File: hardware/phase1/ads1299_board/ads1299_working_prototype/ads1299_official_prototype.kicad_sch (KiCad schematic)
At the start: 105 parts, among them J2 1725656, J3 TSM-110-01-T-DV-P-TR, J5 TSW-103-07-T-D, J6 36PIN_IDC, J80 Conn_02x16_Odd_Even, J81 Conn_02x16_Odd_Even, J9 1725656, U1 ADS1299IPAG, U10 24AA256-I/ST, U11 OPA376AID, U4 OPA376

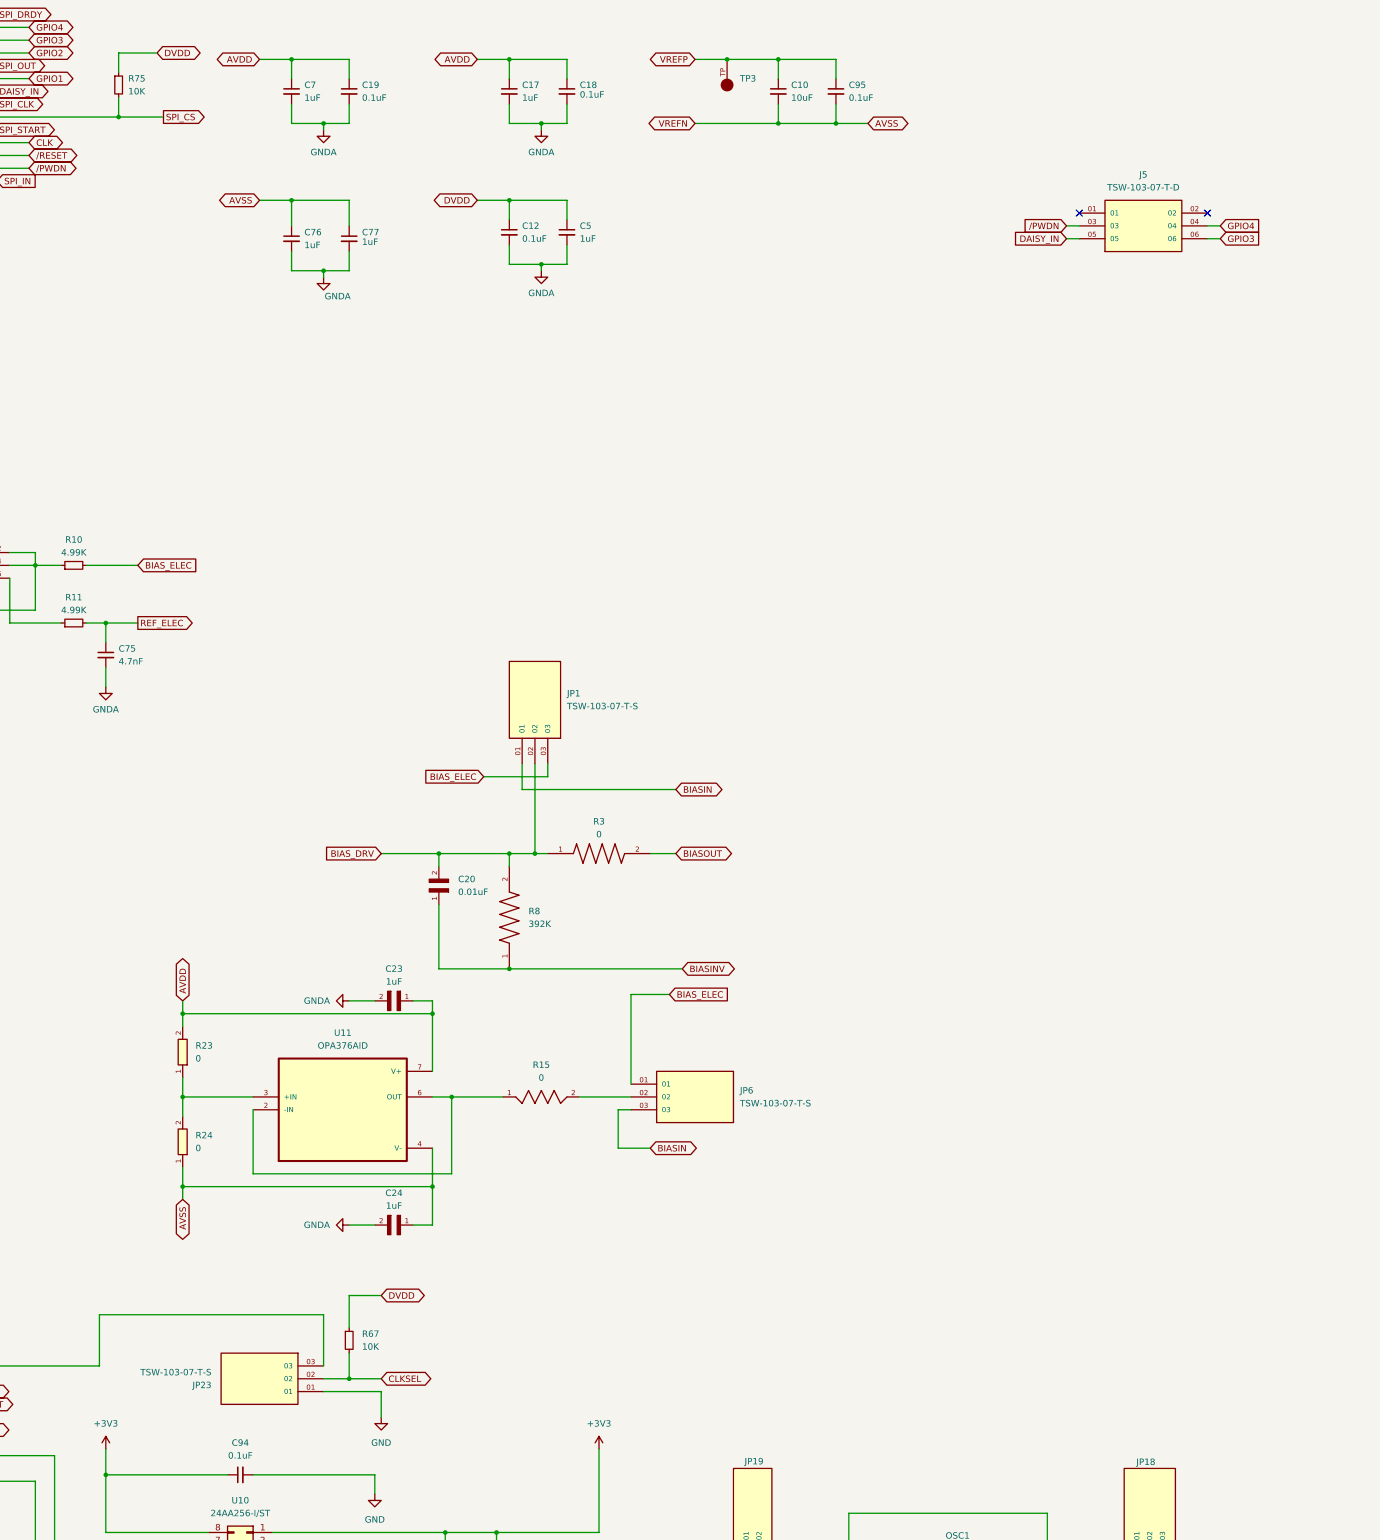
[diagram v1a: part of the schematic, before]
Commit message: Planes are in, need to ask bruno on specifics about them then done
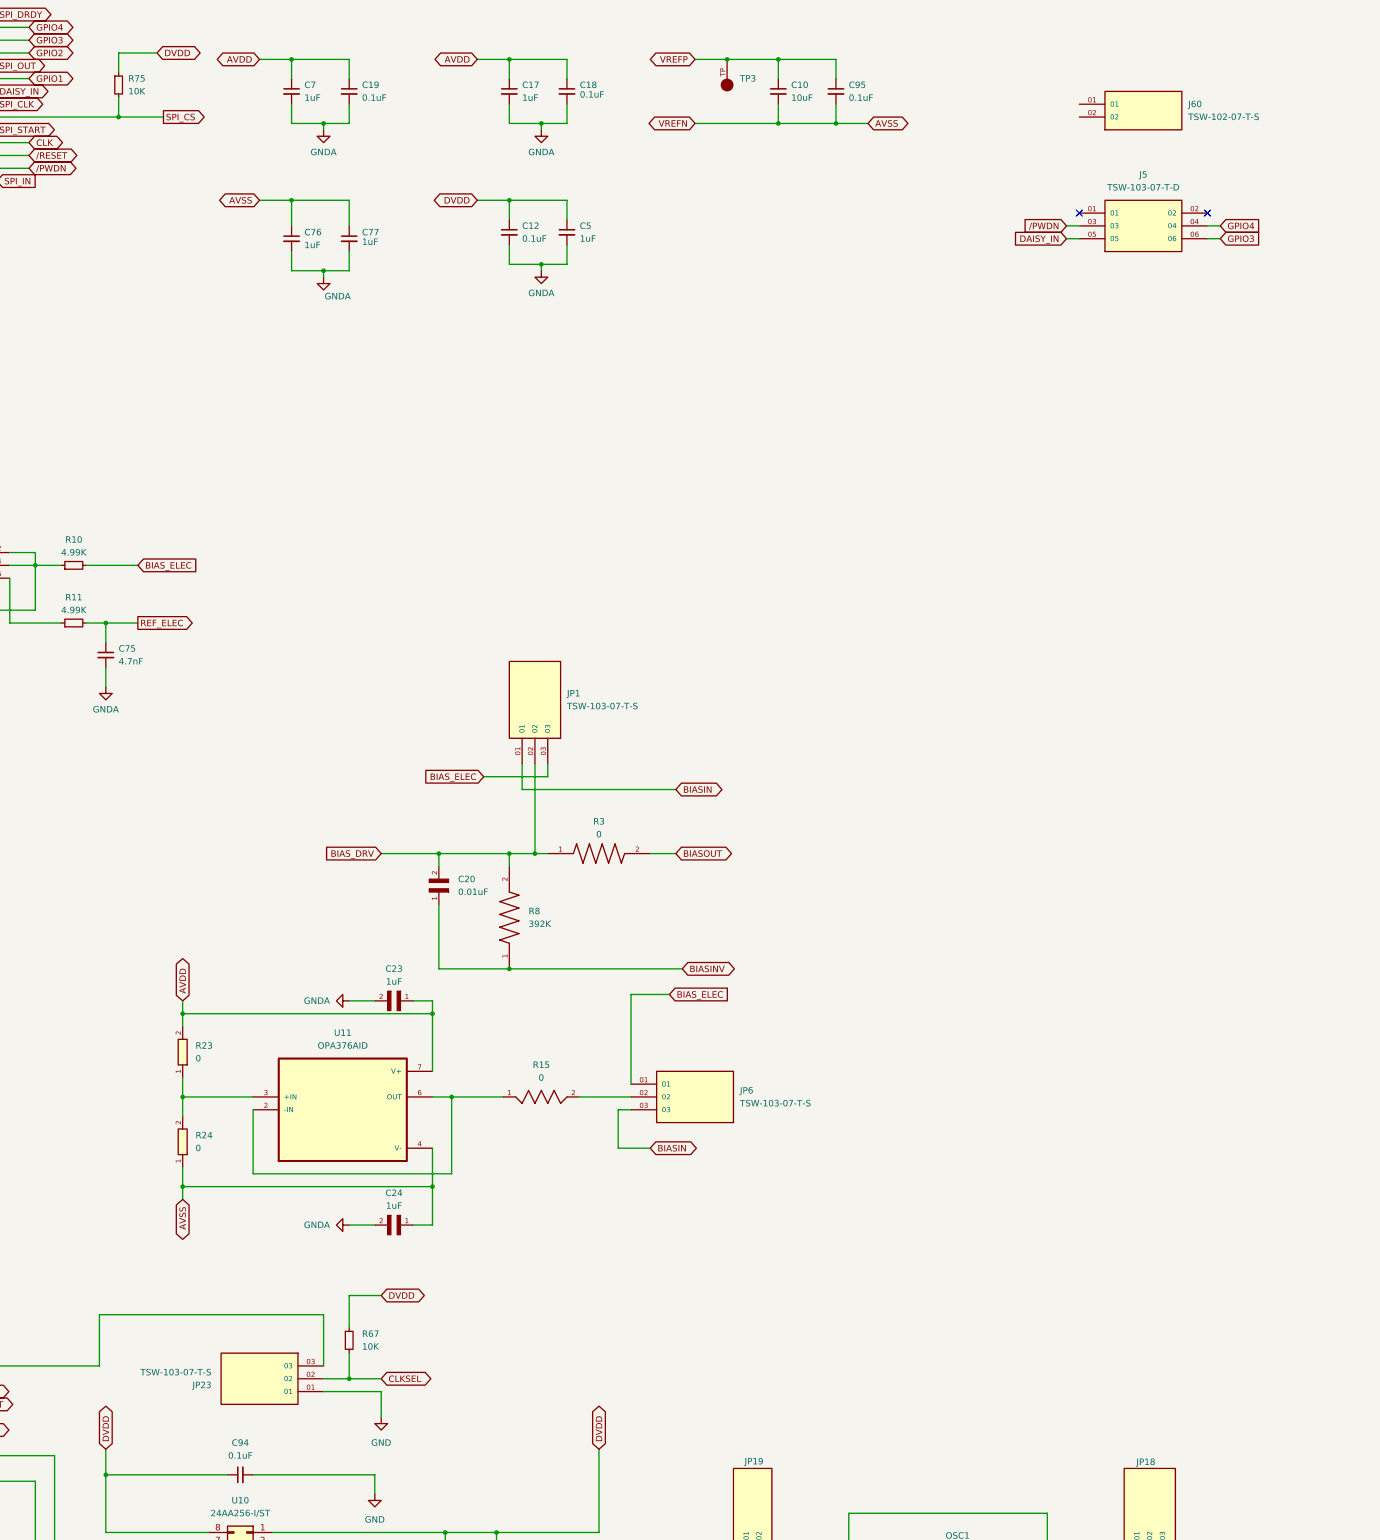
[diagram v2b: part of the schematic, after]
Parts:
- added J60: TSW-102-07-T-S, TSW-102-07-T-S:SAMTEC_TSW-102-07-T-S, symbol TSW-102-07-T-S:TSW-102-07-T-S
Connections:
- net +3V3 is gone; now on net DVDD: C94.1, R71.2, R72.2, R73.2, U10.1 (Pin_1), U10.2 (Pin_2), U10.3 (Pin_3), U10.8 (Pin_8)
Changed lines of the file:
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@@
 		)
 	)
+	(global_label "DVDD"
+		(shape bidirectional)
+		(at 195.58 351.79 90)
+		(fields_autoplaced yes)
+		(effects
+			(font
+				(size 1.27 1.27)
+			)
+			(justify left)
+		)
+		(property "Intersheetrefs" "${INTERSHEET_REFS}"
+			(at 195.58 342.7949 90)
+			(effects
+				(font
+					(size 1.27 1.27)
+				)
+				(justify left)
+				(hide yes)
+			)
+		)
+	)
 	(global_label "17"
 		(shape bidirectional)
@@
 		)
 	)
+	(global_label "DVDD"
+		(shape bidirectional)
+		(at 293.37 351.79 90)
+		(fields_autoplaced yes)
+		(effects
+			(font
+				(size 1.27 1.27)
+			)
+			(justify left)
+		)
+		(property "Intersheetrefs" "${INTERSHEET_REFS}"
+			(at 293.37 342.7949 90)
+			(effects
+				(font
+					(size 1.27 1.27)
+				)
+				(justify left)
+				(hide yes)
+			)
+		)
+	)
 	(global_label "VCAP4"
 		(shape bidirectional)
@@
 	)
 	(symbol
+		(lib_id "TSW-102-07-T-S:TSW-102-07-T-S")
+		(at 401.32 87.63 0)
+		(unit 1)
+		(exclude_from_sim no)
+		(in_bom yes)
+		(on_board yes)
+		(dnp no)
+		(fields_autoplaced yes)
+		(property "Reference" "J60"
+			(at 410.21 85.0899 0)
+			(effects
+				(font
+					(size 1.27 1.27)
+				)
+				(justify left)
+			)
+		)
+		(property "Value" "TSW-102-07-T-S"
+			(at 410.21 87.6299 0)
+			(effects
+				(font
+					(size 1.27 1.27)
+				)
+				(justify left)
+			)
+		)
+		(property "Footprint" "TSW-102-07-T-S:SAMTEC_TSW-102-07-T-S"
+			(at 401.32 87.63 0)
+			(effects
+				(font
+					(size 1.27 1.27)
+				)
+				(justify bottom)
+				(hide yes)
+			)
+		)
+		(property "Datasheet" ""
+			(at 401.32 87.63 0)
+			(effects
+				(font
+					(size 1.27 1.27)
+				)
+				(hide yes)
+			)
+		)
+		(property "Description" ""
+			(at 401.32 87.63 0)
+			(effects
+				(font
+					(size 1.27 1.27)
+				)
+				(hide yes)
+			)
+		)
+		(property "MF" "Samtec"
+			(at 401.32 87.63 0)
+			(effects
+				(font
+					(size 1.27 1.27)
+				)
+				(justify bottom)
+				(hide yes)
+			)
+		)
+		(property "Description_1" "\n                        \n                            TSW - Samtec 2.54mm Pin Header  10.92mm Overall Pin Length (07) - Fast Stock\n                        \n"
+			(at 401.32 87.63 0)
+			(effects
+				(font
+					(size 1.27 1.27)
+				)
+				(justify bottom)
+				(hide yes)
+			)
+		)
+		(property "Package" "None"
+			(at 401.32 87.63 0)
+			(effects
+				(font
+					(size 1.27 1.27)
+				)
+				(justify bottom)
+				(hide yes)
+			)
+		)
+		(property "Price" "None"
+			(at 401.32 87.63 0)
+			(effects
+				(font
+					(size 1.27 1.27)
+				)
+				(justify bottom)
+				(hide yes)
+			)
+		)
+		(property "Check_prices" "https://www.snapeda.com/parts/TSW-102-07-T-S/Samtec/view-part/?ref=eda"
+			(at 401.32 87.63 0)
+			(effects
+				(font
+					(size 1.27 1.27)
+				)
+				(justify bottom)
+				(hide yes)
+			)
+		)
+		(property "STANDARD" "Manufacturer Recommendations"
+			(at 401.32 87.63 0)
+			(effects
+				(font
+					(size 1.27 1.27)
+				)
+				(justify bottom)
+				(hide yes)
+			)
+		)
+		(property "PARTREV" "R"
+			(at 401.32 87.63 0)
+			(effects
+				(font
+					(size 1.27 1.27)
+				)
+				(justify bottom)
+				(hide yes)
+			)
+		)
+		(property "SnapEDA_Link" "https://www.snapeda.com/parts/TSW-102-07-T-S/Samtec/view-part/?ref=snap"
+			(at 401.32 87.63 0)
+			(effects
+				(font
+					(size 1.27 1.27)
+				)
+				(justify bottom)
+				(hide yes)
+			)
+		)
+		(property "MP" "TSW-102-07-T-S"
+			(at 401.32 87.63 0)
+			(effects
+				(font
+					(size 1.27 1.27)
+				)
+				(justify bottom)
+				(hide yes)
+			)
+		)
+		(property "Availability" "In Stock"
+			(at 401.32 87.63 0)
+			(effects
+				(font
+					(size 1.27 1.27)
+				)
+				(justify bottom)
+				(hide yes)
+			)
+		)
+		(property "MANUFACTURER" "Samtec"
+			(at 401.32 87.63 0)
+			(effects
+				(font
+					(size 1.27 1.27)
+				)
+				(justify bottom)
+				(hide yes)
+			)
+		)
+		(pin "01"
+		)
+		(pin "02"
+		)
+		(instances
+			(project ""
+				(path "/0ef51407-3c01-447a-a681-0fc3deaf4e2b"
+					(reference "J60")
+					(unit 1)
+				)
+			)
+		)
+	)
+	(symbol
 		(lib_id "power:GNDA")
 		(at 165.1 373.38 0)
@@
 	)
 	(symbol
-		(lib_id "power:+3V3")
-		(at 293.37 351.79 0)
-		(mirror y)
-		(unit 1)
-		(exclude_from_sim no)
-		(in_bom yes)
-		(on_board yes)
-		(dnp no)
-		(fields_autoplaced yes)
-		(property "Reference" "#PWR040"
-			(at 293.37 355.6 0)
-			(effects
-				(font
-					(size 1.27 1.27)
-				)
-				(hide yes)
-			)
-		)
-		(property "Value" "+3V3"
-			(at 293.37 346.71 0)
-			(effects
-				(font
-					(size 1.27 1.27)
-				)
-			)
-		)
-		(property "Footprint" ""
-			(at 293.37 351.79 0)
-			(effects
-				(font
-					(size 1.27 1.27)
-				)
-				(hide yes)
-			)
-		)
-		(property "Datasheet" ""
-			(at 293.37 351.79 0)
-			(effects
-				(font
-					(size 1.27 1.27)
-				)
-				(hide yes)
-			)
-		)
-		(property "Description" "Power symbol creates a global label with name \"+3V3\""
-			(at 293.37 351.79 0)
-			(effects
-				(font
-					(size 1.27 1.27)
-				)
-				(hide yes)
-			)
-		)
-		(pin "1"
-		)
-		(instances
-			(project "ads1299_official_prototype"
-				(path "/0ef51407-3c01-447a-a681-0fc3deaf4e2b"
-					(reference "#PWR040")
-					(unit 1)
-				)
-			)
-		)
-	)
-	(symbol
 		(lib_id "power:GNDA")
 		(at 128.27 294.64 270)
@@
 					(unit 1)
 				)
-			)
-		)
-	)
-	(symbol
-		(lib_id "power:+3V3")
-		(at 195.58 351.79 0)
-		(unit 1)
-		(exclude_from_sim no)
-		(in_bom yes)
-		(on_board yes)
-		(dnp no)
-		(fields_autoplaced yes)
-		(property "Reference" "#PWR036"
-			(at 195.58 355.6 0)
-			(effects
-				(font
-					(size 1.27 1.27)
-				)
-				(hide yes)
-			)
-		)
-		(property "Value" "+3V3"
-			(at 195.58 346.71 0)
-			(effects
-				(font
-					(size 1.27 1.27)
-				)
-			)
-		)
-		(property "Footprint" ""
-			(at 195.58 351.79 0)
-			(effects
-				(font
-					(size 1.27 1.27)
-				)
-				(hide yes)
-			)
-		)
-		(property "Datasheet" ""
-			(at 195.58 351.79 0)
-			(effects
-				(font
-					(size 1.27 1.27)
-				)
-				(hide yes)
-			)
-		)
-		(property "Description" "Power symbol creates a global label with name \"+3V3\""
-			(at 195.58 351.79 0)
-			(effects
-				(font
-					(size 1.27 1.27)
-				)
-				(hide yes)
-			)
-		)
-		(pin "1"
-		)
-		(instances
-			(project ""
-				(path "/0ef51407-3c01-447a-a681-0fc3deaf4e2b"
-					(reference "#PWR036")
-					(unit 1)
-				)

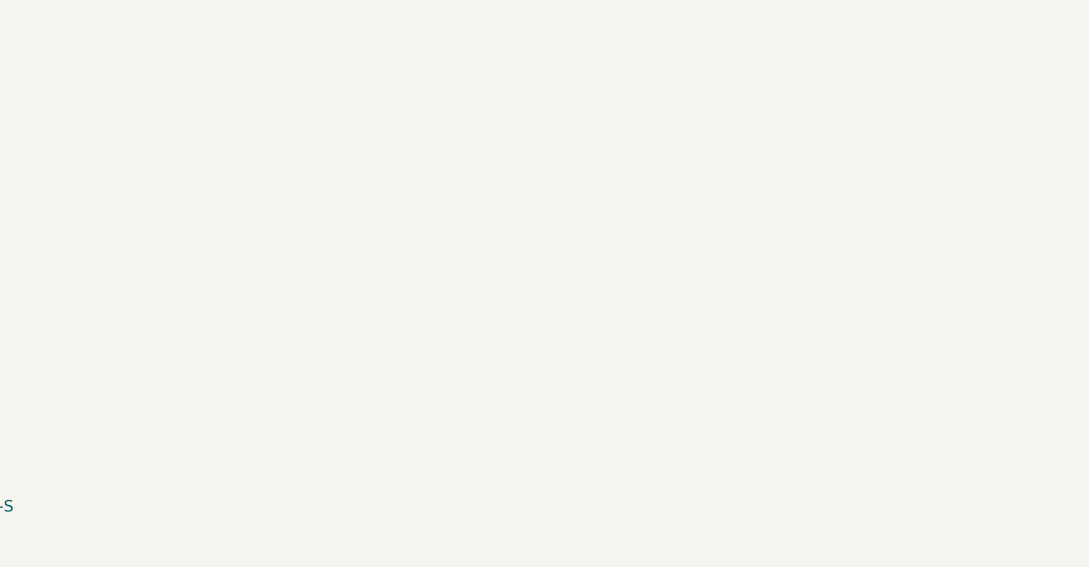
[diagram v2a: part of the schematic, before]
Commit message: DONE, but need to edit some footprints and add the biasref header
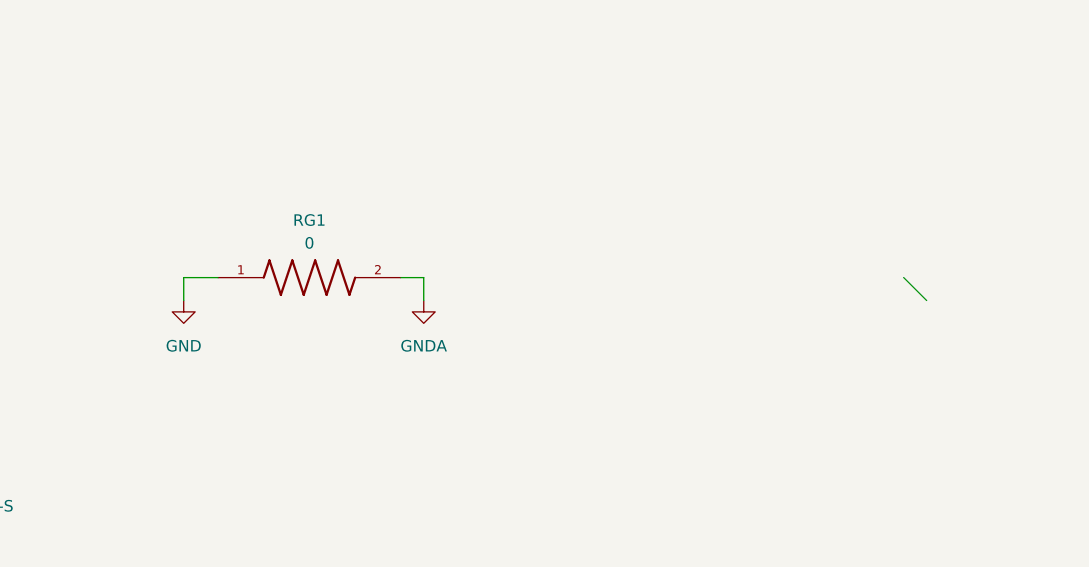
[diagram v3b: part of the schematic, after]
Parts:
- added RG1: 0, RC0603JR-070RL:RESC1607X60N, symbol RC0603JR-070RL:RC0603JR-070RL
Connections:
- net GND: now also RG1.1
- net GNDA: now also RG1.2

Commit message: Chat it's done
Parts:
- removed J60: TSW-102-07-T-S, TSW-102-07-T-S:SAMTEC_TSW-102-07-T-S, symbol TSW-102-07-T-S:TSW-102-07-T-S
- removed J80, J81: Conn_02x16_Odd_Even, symbol Connector_Generic:Conn_02x16_Odd_Even
- removed U1: ADS1299IPAG, ADS1299CPAG:QFP64P50_1200X1200X120L60X22N, symbol ADS1299IPAG:ADS1299IPAG
- added IC1: ADS1299-4PAGR, QFP50P1200X1200X120-64N, symbol ADS1299-4PAGR:ADS1299-4PAGR
- added JP60: TSW-103-07-T-S, TSW-103-07-T-S:SAMTEC_TSW-103-07-T-S, symbol TSW-103-07-T-S:TSW-103-07-T-S
- added TPAVDD1: AVDD, 5000:KEYSTONE_5000, symbol 5000:5000
- added TPAVSS1: AVSS, 5000:KEYSTONE_5000, symbol 5000:5000
- added TPDVDD1: DVDD, 5000:KEYSTONE_5000, symbol 5000:5000
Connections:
- net AIN1N: now also IC1.15 (IN1N)
- net AIN1P: now also IC1.16 (IN1P)
- net AIN2N: now also IC1.13 (IN2N)
- net AIN2P: now also IC1.14 (IN2P)
- net AIN3N: now also IC1.11 (IN3N)
- net AIN3P: now also IC1.12 (IN3P)
- net AIN4N: now also IC1.9 (IN4N)
- net AIN4P: now also IC1.10 (IN4P)
- net AIN5N: now also IC1.7 (IN5N)
- net AIN5P: now also IC1.8 (IN5P)
- net AIN6N: now also IC1.5 (IN6N)
- net AIN6P: now also IC1.6 (IN6P)
- net AIN7N: now also IC1.3 (IN7N)
- net AIN7P: now also IC1.4 (IN7P)
- net AIN8N: now also IC1.1 (IN8N)
- net AIN8P: now also IC1.2 (IN8P)
- net AVDD: now also IC1.19 (AVDD_1), IC1.21 (AVDD_2), IC1.22 (AVDD_3), IC1.54 (AVDD1), IC1.56 (AVDD_4), IC1.59 (AVDD_5), JP60.03, TPAVDD1.TP
- net AVSS: now also IC1.20 (AVSS_1), IC1.23 (AVSS_2), IC1.25 (VREFN), IC1.32 (AVSS_3), IC1.53 (AVSS1), IC1.57 (AVSS_4), IC1.58 (AVSS_5), JP60.01, TPAVSS1.TP
- net BIASIN: now also IC1.62 (BIASIN)
- net BIASINV: now also IC1.61 (BIASINV)
- net BIASOUT: now also IC1.63 (BIASOUT)
- net BIASREF: now also IC1.60 (BIASREF), JP60.02
- net CLK: now also IC1.37 (CLK)
- net CLKSEL: now also IC1.52 (CLKSEL)
- net DAISY_IN: now also IC1.41 (DAISY_IN)
- net DVDD: now also IC1.48 (DVDD_1), IC1.50 (DVDD_2), TPDVDD1.TP
- net GNDA: now also IC1.31 (RESV1), IC1.33 (DGND_1), IC1.49 (DGND_2), IC1.51 (DGND_3), IC1.64 (RESERVED)
- net GPIO1: now also IC1.42 (GPIO1)
- net GPIO2: now also IC1.44 (GPIO2)
- net GPIO3: now also IC1.45 (GPIO3)
- net GPIO4: now also IC1.46 (GPIO4)
- net SPI_CLK: now also IC1.40 (SCLK)
- net SPI_CS: now also IC1.39 (~{CS})
- net SPI_DRDY: now also IC1.47 (~{DRDY})
- net SPI_IN: now also IC1.34 (DIN)
- net SPI_OUT: now also IC1.43 (DOUT)
- net SPI_START: now also IC1.38 (START)
- net SRB1: now also IC1.17 (SRB1)
- net SRB2: now also IC1.18 (SRB2)
- net VCAP1: now also IC1.28 (VCAP1)
- net VCAP2: now also IC1.30 (VCAP2)
- net VCAP3: now also IC1.55 (VCAP3)
- net VCAP4: now also IC1.26 (VCAP4)
- net VREFP: now also IC1.24 (VREFP)
- net /PWDN: now also IC1.35 (~{PWDN})
- net /RESET: now also IC1.36 (~{RESET})
- no-connect marks 33 -> 9
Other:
- moved on the sheet: C1, C10, C12, C13, C14, C15, C16, C17, C18, C19, C2, C3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

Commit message: Okay done
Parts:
- removed RG1: 0, RC0603JR-070RL:RESC1607X60N, symbol RC0603JR-070RL:RC0603JR-070RL
- added FB1: FCM_1608KF-601T03, BEADC1608X95N, symbol FCM_1608KF-601T03:FCM_1608KF-601T03
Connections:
- net GND: now also FB1.1
- net GNDA: now also FB1.2
